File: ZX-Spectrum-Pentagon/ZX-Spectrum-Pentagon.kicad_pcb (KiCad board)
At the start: 2 copper layers, 213.1 x 129 mm, 250 parts, among them U1 74HC04, U10 74HC193, U11 74HC02, U12 74HC08, U13 74HC74, U14 74HC393, U15 74HC74, U16 74HC273, U17 74HC257, U18 74HC273, U19 AY-3-8910, U2 74HC14, U20 AY-3-8912_DUMMY, U21 AY-3-8913_DUMMY, U22 LM311, U23 74HC244, U25 74HC541, U26 74HC541, U27 Z80CPU, U28 74HC244, U29 GAL16V8, U3 74HC93, U30 29F040, U31 74HC32, U32 74HC00, U33 74HC74, U34 74HC08, U35 74HC574, U36 74HC574, U37 74HC153, U38 74HC153, U39 GAL16V8, U4 74HC11, U40 74HC574, U41 74HC166, U42 74HC257, U43 74HC541, U44 HM628512, U45 74HC574, U46 74HC257, U47 74HC257, U48 74HC257, U49 74HC08, U5 74HC193, U50 AD724, U6 74HC257, U7 74HC04, U8 74HC00, U9 74HC86

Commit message: reposition companents, add some class net
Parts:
- JIO2, JIO3: value AudioJack -> SJ1 - 353 5 NG
- JIO4: footprint Connector_PinSocket_2.54mm:PinSocket_1x02_P2.54mm_Vertical -> Connector_PinHeader_2.54mm:PinHeader_1x02_P2.54mm_Vertical
- JIOA1, JIOB1: footprint Connector_PinSocket_2.54mm:PinSocket_1x08_P2.54mm_Vertical -> Connector_PinHeader_2.54mm:PinHeader_1x08_P2.54mm_Vertical
- moved JIOKB1 399.8 mm to (51.3, 97.5), turned to 90 degrees
- moved RIO10 345.9 mm to (133.3, 96.5)
- moved DIO3 342.4 mm to (108.0, 55.9)
- moved RIO2 337.5 mm to (108.0, 68.6)
- moved DIO1 331.1 mm to (108.0, 58.4)
- moved U22 329.7 mm to (113.0, 59.7)
- moved RIO15 328.9 mm to (128.3, 95.2)
- moved DIO2 326.9 mm to (108.0, 61.0)
- moved RIO3 325.5 mm to (99.1, 64.8)
- moved RIO7 324.8 mm to (100.3, 67.3)
- moved RIO4 321.6 mm to (108.0, 63.5)
- moved CIO6 319.0 mm to (66.0, 21.6), turned to 180 degrees
- moved RIO16 317.4 mm to (104.1, 53.3)
- moved CPF22 316.8 mm to (118.1, 57.1)
- moved CIO7 311.4 mm to (104.1, 55.9)
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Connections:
- U3 pad 13: (no net) -> unconnected-(U3-Pad13)
- U3 pad 4: (no net) -> unconnected-(U3-Pad4)
- U3 pad 6: (no net) -> unconnected-(U3-Pad6)
- U3 pad 7: (no net) -> unconnected-(U3-Pad7)
- locked pad 1: /CPU/BUSACK -> /CPU/~{DIR}
- locked pad 19: /CPU/~{DIR} -> /CPU/BUSACK

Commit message: merge with stash
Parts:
- QG1: footprint Package_TO_SOT_SMD:SOT-23_Handsoldering -> Package_TO_SOT_SMD:SOT-323_SC-70_Handsoldering
- moved RIO8 100.1 mm to (85.1, 22.9)
- moved RIO14 95.0 mm to (71.1, 22.9), turned to 180 degrees
- moved RIO15 90.7 mm to (71.1, 24.8)
- moved RIO11 90.3 mm to (71.1, 28.6), turned to 180 degrees
- moved RIO10 89.4 mm to (71.1, 32.4), turned to 180 degrees
- moved RIO13 88.9 mm to (71.1, 26.7), turned to 180 degrees
- moved CIO9 87.5 mm to (72.4, 50.8), turned to -90 degrees
- moved CIO3 77.6 mm to (85.1, 26.7), turned to 180 degrees
- moved CIO4 74.9 mm to (85.1, 28.6), turned to 180 degrees
- moved CIO11 73.7 mm to (80.0, 38.1), turned to -90 degrees
- moved RIO1 48.6 mm to (71.1, 34.3), turned to 180 degrees
- moved RIO2 47.8 mm to (71.1, 38.1), turned to 180 degrees
- moved RIO16 40.2 mm to (71.1, 30.5)
- moved RIO4 40.2 mm to (85.1, 30.5), turned to 180 degrees
- moved DIO3 40.1 mm to (69.9, 43.2), turned to 90 degrees
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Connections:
- RIO13 pad 2: Net-(RIO13-Pad2) -> Net-(CIO12-Pad1)
- RIO15 pad 1: Net-(RIO13-Pad2) -> Net-(CIO12-Pad1)
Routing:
- net GND: vias 0 -> 6
- net (no net): vias 6 -> 0

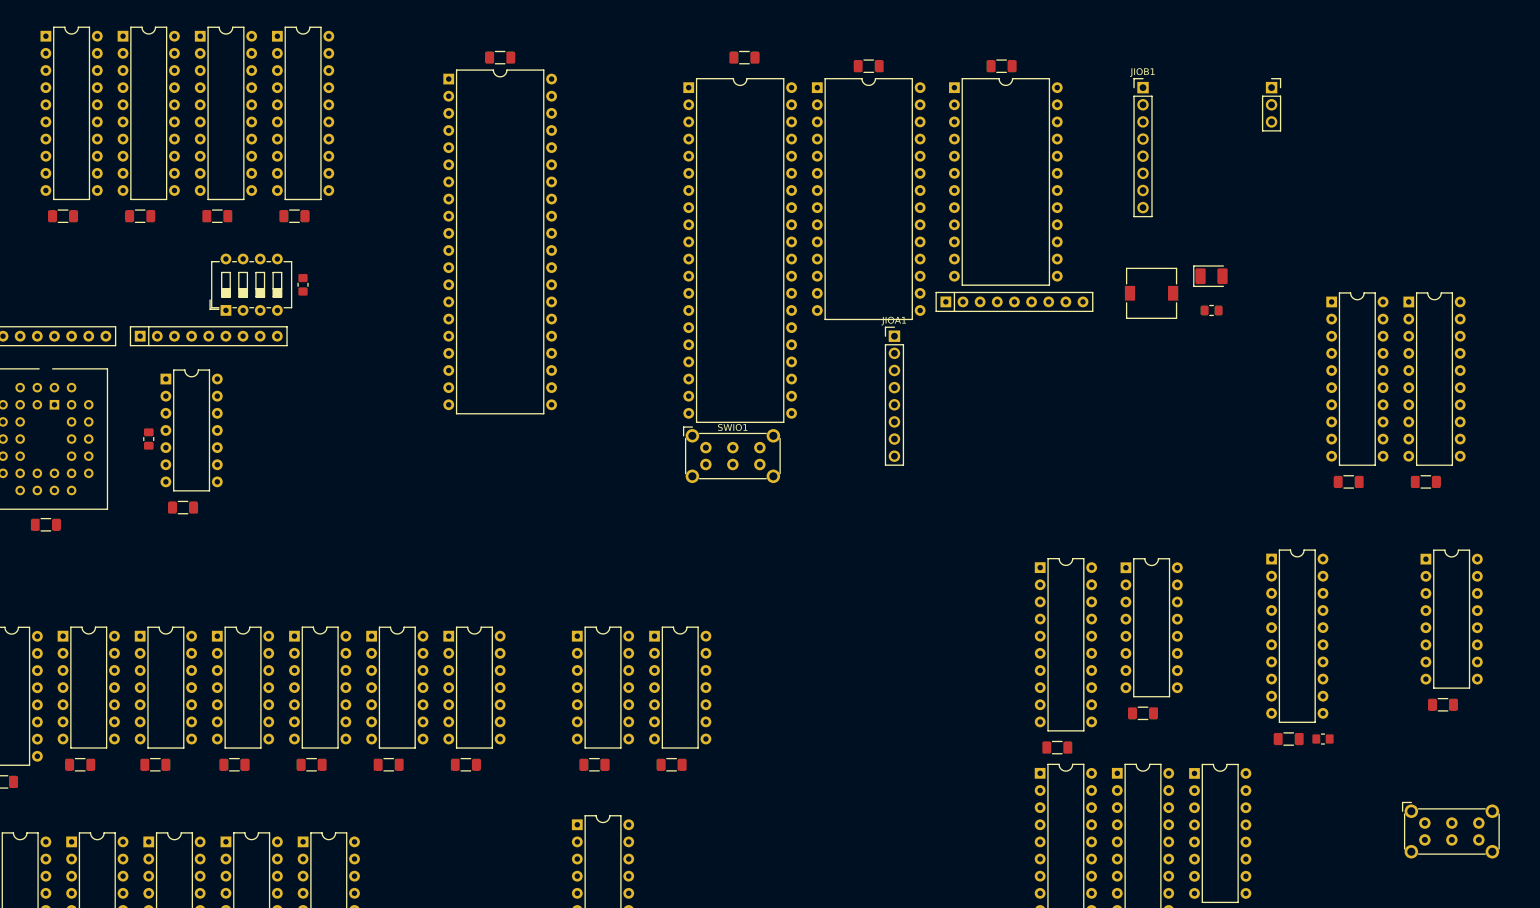
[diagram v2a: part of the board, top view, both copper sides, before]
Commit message: fix some conflicts and reposition components
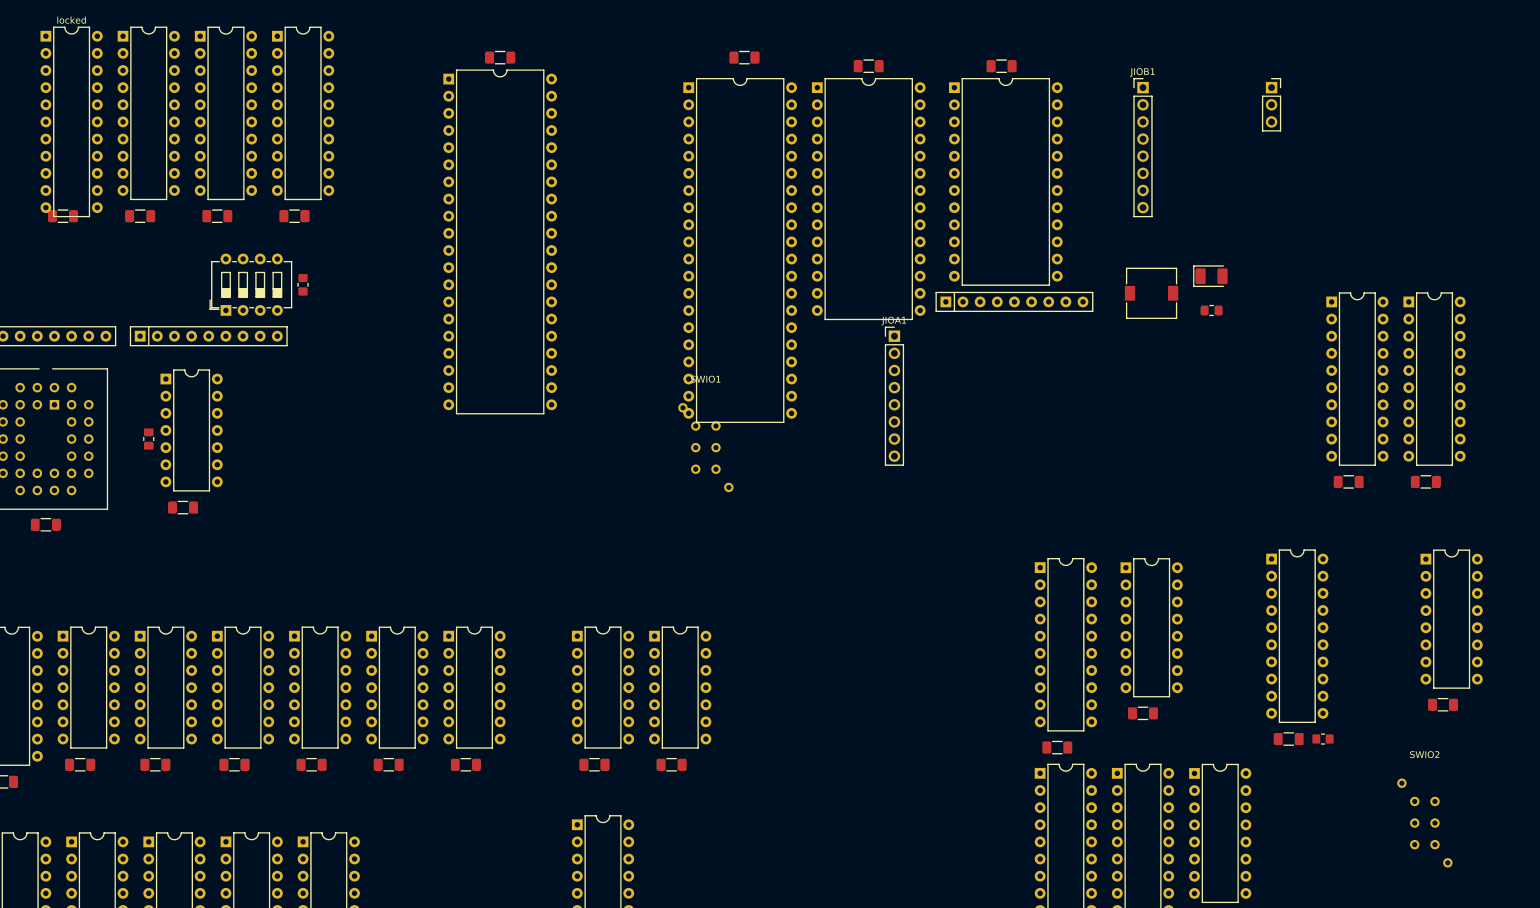
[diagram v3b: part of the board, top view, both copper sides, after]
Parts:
- SWIO1, SWIO2: footprint Button_Switch_THT:SW_E-Switch_EG2219_DPDT_Angled -> ZX-Spectrum-Pentagon:PS-22F03
- locked: footprint Package_DIP:DIP-20_W7.62mm -> Package_DIP:DIP-22_W7.62mm
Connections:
- U34 pad 10: /MX3 -> /GPA7
- U34 pad 11: /Memory/MA17 -> (no net)
- U34 pad 12: Net-(U34-Pad12) -> (no net)
- U34 pad 13: /GPA6 -> (no net)
- U34 pad 8: Net-(U34-Pad12) -> /Memory/MA18
- U34 pad 9: /CPU -> Net-(U34-Pad9)
- U49 pad 1: Net-(U34-Pad12) -> /CPU
- U49 pad 2: /GPA7 -> /MX3
- U49 pad 3: /Memory/MA18 -> Net-(U34-Pad9)
- U49 pad 4: (no net) -> Net-(U34-Pad9)
- U49 pad 5: (no net) -> /GPA6
- U49 pad 6: (no net) -> /Memory/MA17

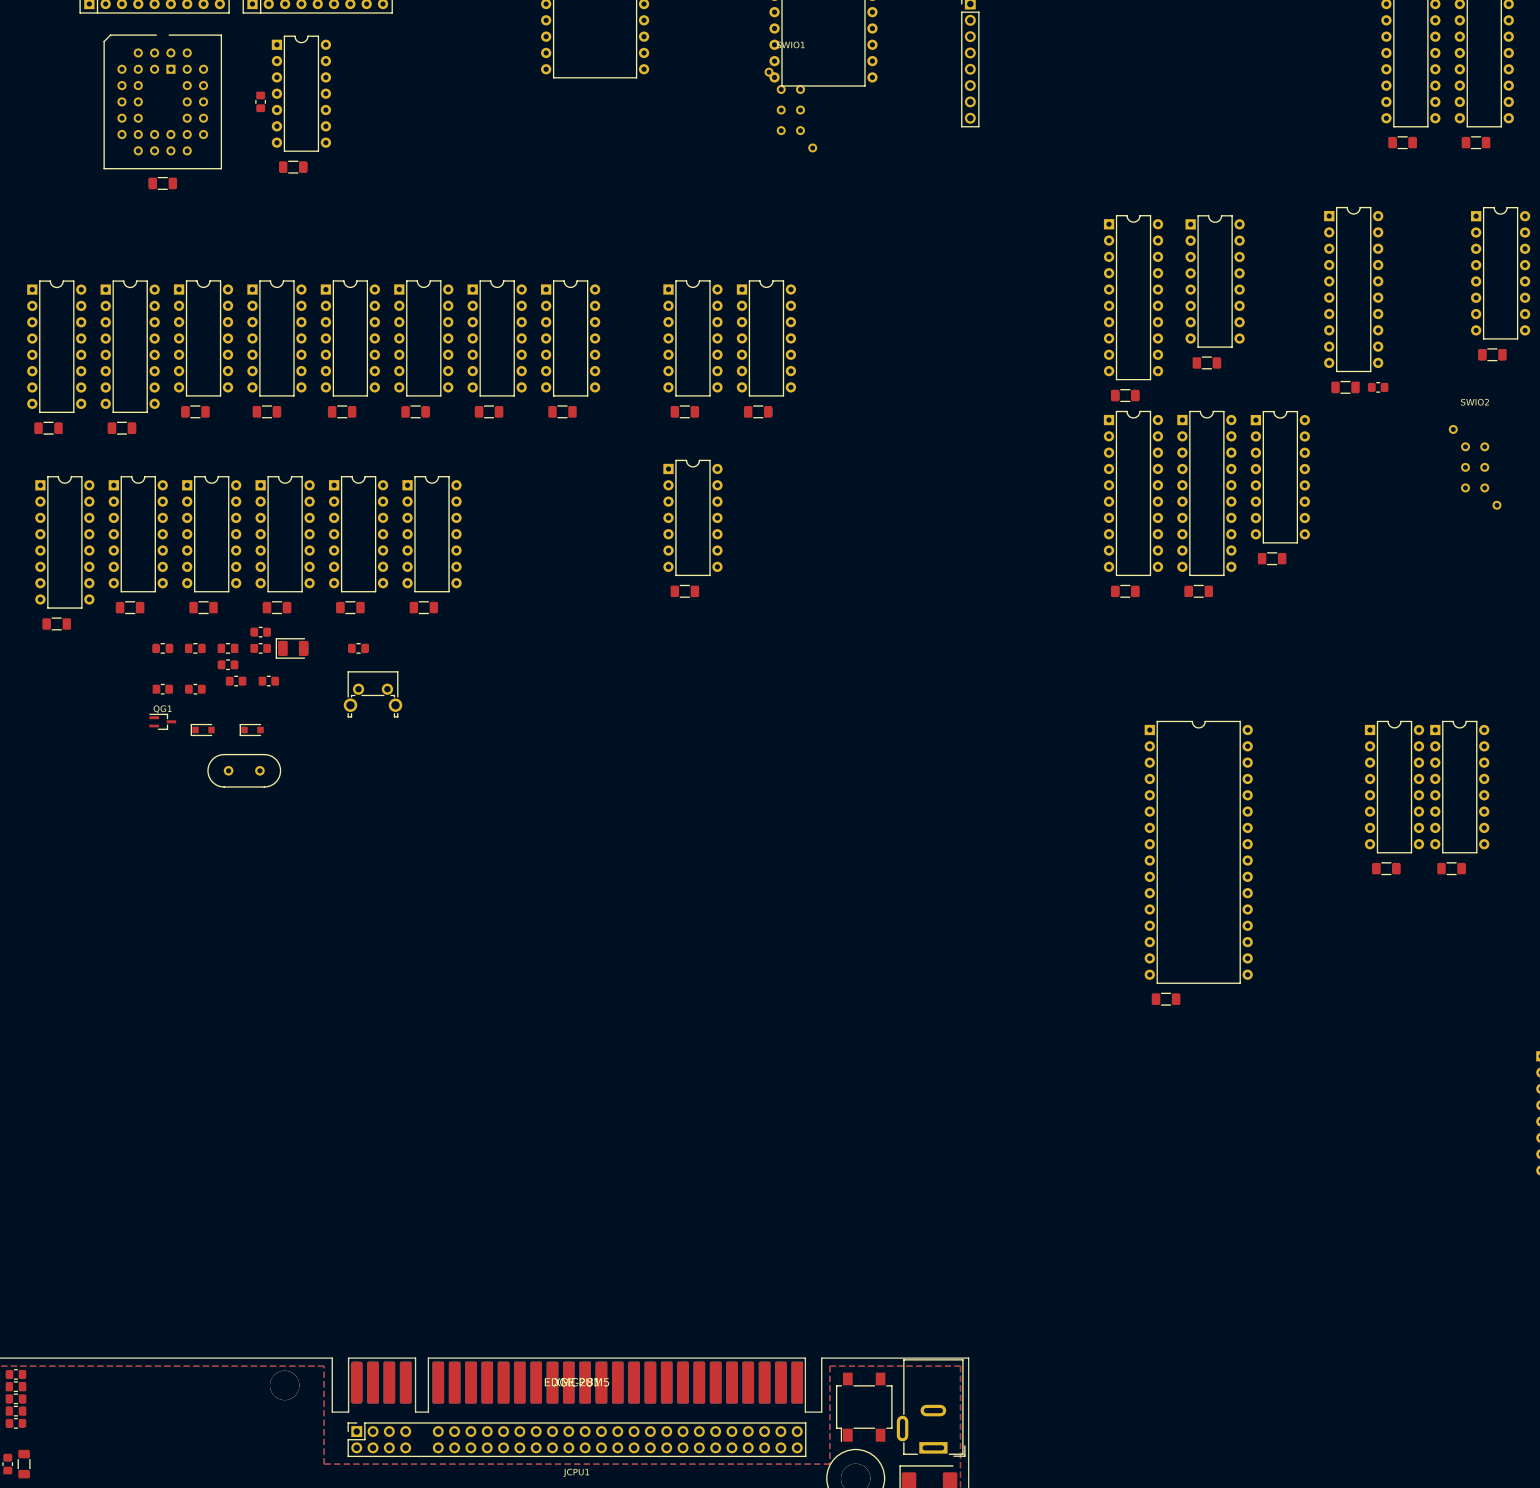
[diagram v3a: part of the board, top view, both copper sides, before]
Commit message: reposition companents
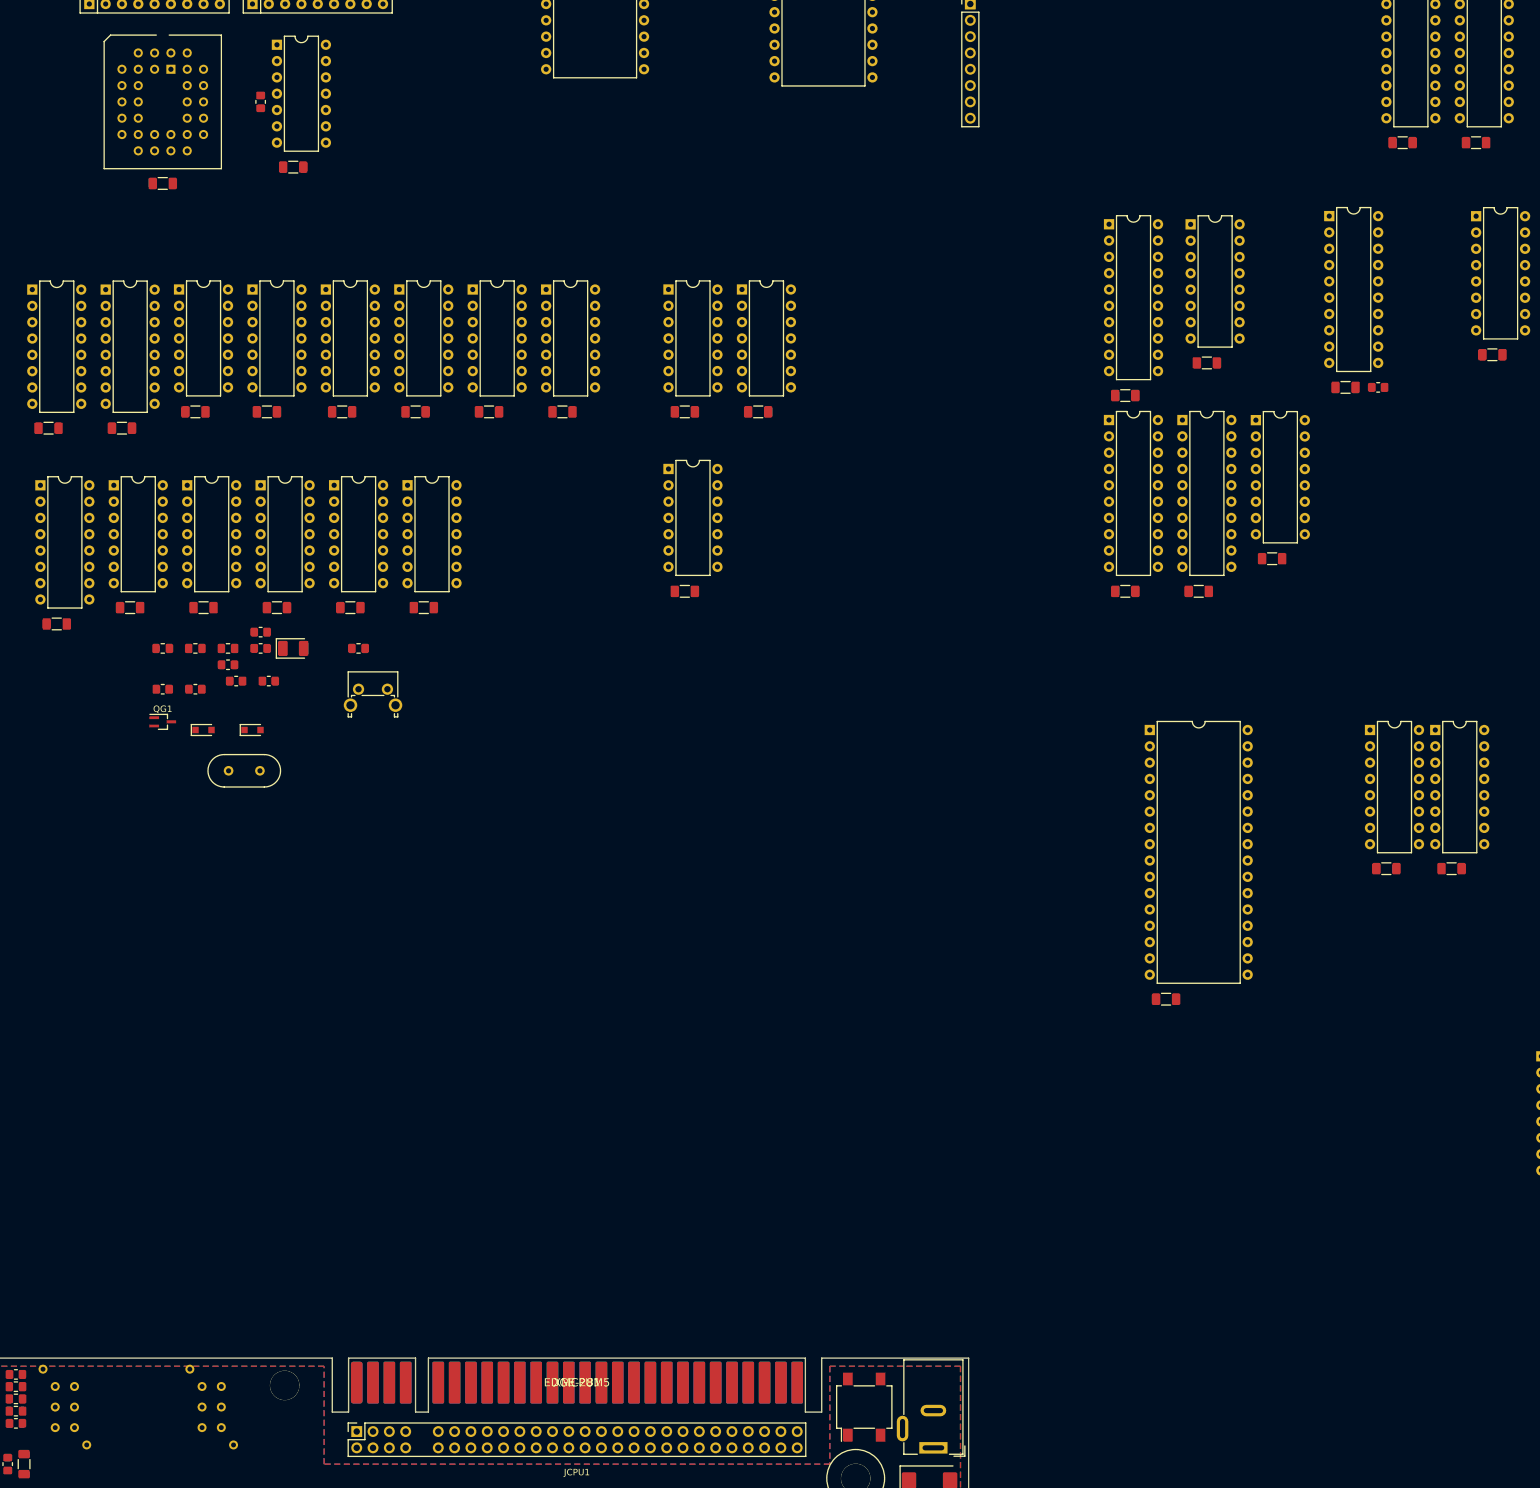
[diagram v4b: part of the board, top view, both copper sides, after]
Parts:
- moved SWIO2 245.1 mm to (115.6, 27.9)
- moved SWIO1 231.4 mm to (92.7, 27.9)
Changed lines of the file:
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@@
   )
   (footprint "ZX-Spectrum-Pentagon:PS-22F03" (layer "F.Cu")
-    (at 312.2725 -118.3625)
+    (at 115.57 27.94)
     (property "Sheetfile" "VideoFormating.kicad_sch")
     (property "Sheetname" "VideoFormating")
     (attr through_hole)
-    (fp_text reference "SWIO2" (at 0 -10.1 unlocked) (layer "F.SilkS")
+    (fp_text reference "SWIO2" (at 0 -10.1 unlocked) (layer "F.SilkS") hide
       (effects (font (size 1 1) (thickness 0.15)))
     )
-    (fp_text value "SW_Push_DPDT" (at 0 9.2 unlocked) (layer "F.Fab")
+    (fp_text value "SW_Push_DPDT" (at 0 9.2 unlocked) (layer "F.Fab") hide
       (effects (font (size 1 1) (thickness 0.15)))
     )
-    (fp_text user "${REFERENCE}" (at 0 10.7 unlocked) (layer "F.Fab")
-      (effects (font (size 1 1) (thickness 0.15)))
+    (fp_text user "${REFERENCE}" (at 0 0.55 90 unlocked) (layer "F.Fab")
+      (effects (font (size 3 3) (thickness 0.15)))
     )
     (fp_line (start 4.1 6.6) (end 4.1 -6.6) (layer "Eco2.User") (width 0.12))
@@
   )
   (footprint "ZX-Spectrum-Pentagon:PS-22F03" (layer "F.Cu")
-    (at 205.74 -173.99)
+    (at 92.71 27.94)
     (property "Sheetfile" "InputOutput.kicad_sch")
     (property "Sheetname" "InputOutput")
     (attr through_hole)
-    (fp_text reference "SWIO1" (at 0 -10.1 unlocked) (layer "F.SilkS")
+    (fp_text reference "SWIO1" (at 0 -10.1 unlocked) (layer "F.SilkS") hide
       (effects (font (size 1 1) (thickness 0.15)))
     )
-    (fp_text value "SW_Push_DPDT" (at 0 9.2 unlocked) (layer "F.Fab")
+    (fp_text value "SW_Push_DPDT" (at 0 9.2 unlocked) (layer "F.Fab") hide
       (effects (font (size 1 1) (thickness 0.15)))
     )
-    (fp_text user "${REFERENCE}" (at 0 10.7 unlocked) (layer "F.Fab")
-      (effects (font (size 1 1) (thickness 0.15)))
+    (fp_text user "${REFERENCE}" (at 0 0 90 unlocked) (layer "F.Fab")
+      (effects (font (size 3 3) (thickness 0.15)))
     )
     (fp_line (start -4.1 6.6) (end 4.1 6.6) (layer "Eco2.User") (width 0.12))
@@
     (connect_pads (clearance 0.508))
     (min_thickness 0.254)
-    (fill (thermal_gap 0.508) (thermal_bridge_width 0.508))
+    (fill yes (thermal_gap 0.508) (thermal_bridge_width 0.508))
     (polygon
       (pts
@@
     (connect_pads (clearance 0.508))
     (min_thickness 0.254)
-    (fill (thermal_gap 0.508) (thermal_bridge_width 0.508))
+    (fill yes (thermal_gap 0.508) (thermal_bridge_width 0.508))
     (polygon
       (pts
